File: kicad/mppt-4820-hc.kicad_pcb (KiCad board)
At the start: 4 copper layers, 100 x 100 mm, 141 parts, among them J1 MKDS 5/ 2-9,5, J2 MKDS 5/ 2-9,5, J4 8P8C, J5 8P8C, J7 UEXT, P1 CONN_01X02, Q1 IPA045N10N3G, Q2 IPA045N10N3G, Q3 IPA045N10N3G, T1 BC846B, T10 BC846B, T3 BC846B, T4 BC856B, U1 LM5107, U2 STM32G431CBTx, U3 MPQ8112, U4 LMR16006X, U6 W25Q80DVS, U7 TCAN334, Y1 8MHz

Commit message: pcb minor fixes, updated bom files, updated project name
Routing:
- net /CAN_GND: track 129.5 -> 127.1 mm
- net /CAN/CAN_PWR1: track 103.0 -> 100.8 mm
- net VBUS: vias 20 -> 24
- net /BAT+: vias 4 -> 8
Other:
- board text added: "MPPT 4820 HC"
- board text added: "v0.1.0"
- board text removed: "MPPT 2420 HC"
- board text removed: "v0.2.3"

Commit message: minor fixes & cleanup
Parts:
- moved J2 0.12 mm to (145.2, 132.0)
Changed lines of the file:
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@@
   )
   (footprint "LibreSolar:Phoenix_Contact_MKDS_5-2-9,5" (layer "F.Cu")
-    (at 145.139 132.05)
+    (at 145.25 132)
     (descr "Phoenix Contact MKDS 5/2-9,52")
     (property "Manufacturer" "Phoenix Contact")

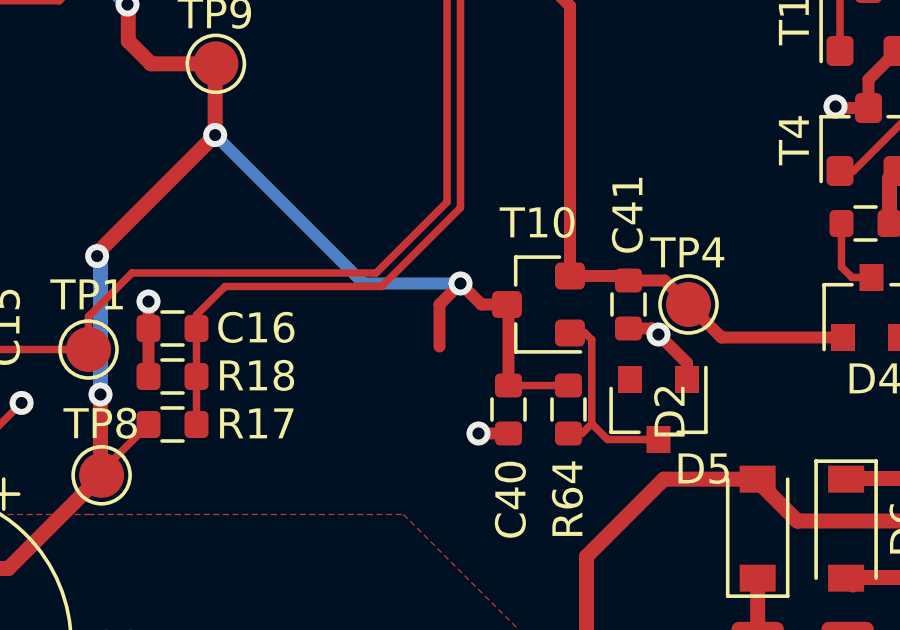
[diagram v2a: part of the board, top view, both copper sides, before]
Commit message: updated project to kicad 7
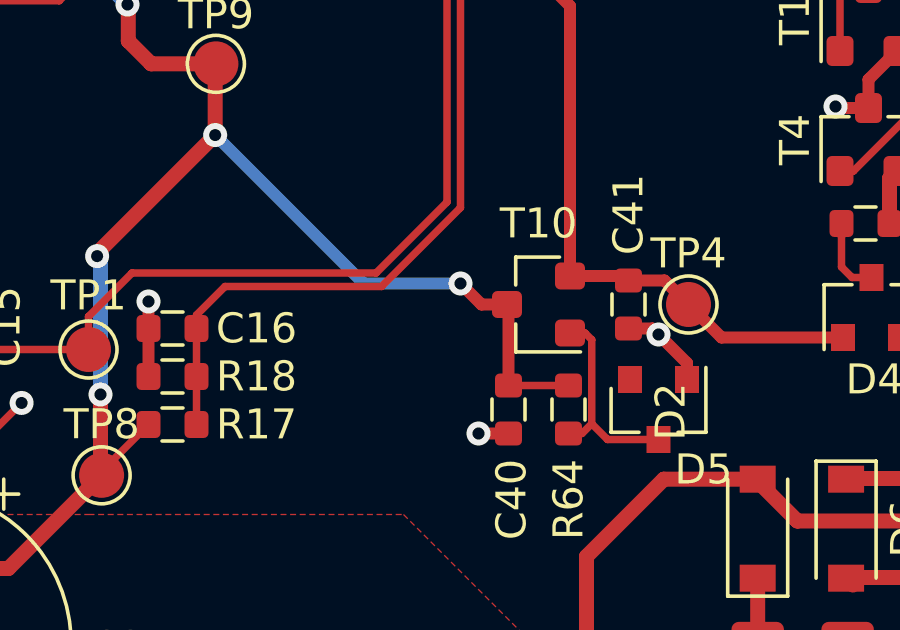
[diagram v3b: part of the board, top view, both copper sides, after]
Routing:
- net VBUS: track 124.3 -> 122.0 mm

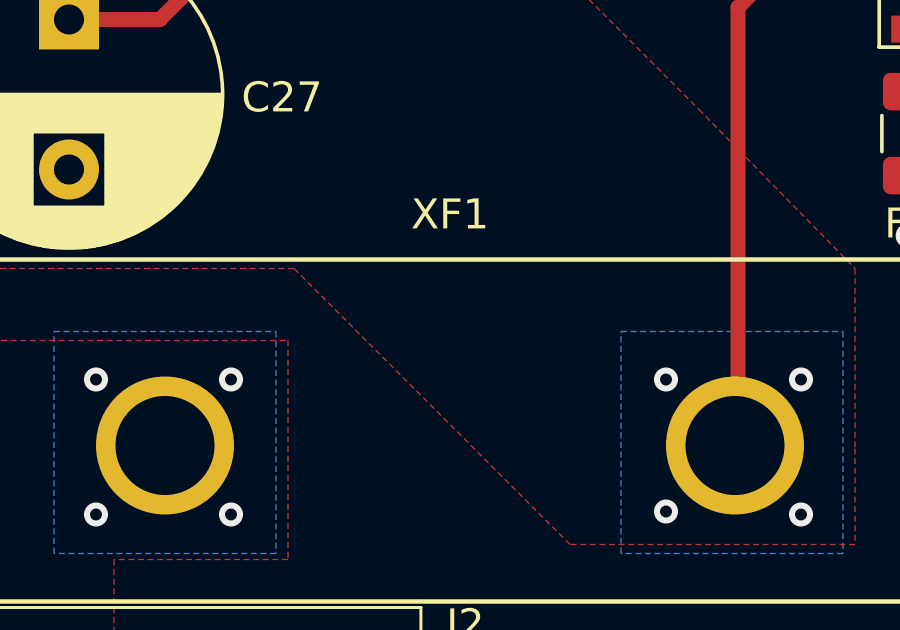
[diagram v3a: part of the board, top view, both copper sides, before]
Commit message: some DRC check errors fixes (prototype 1)
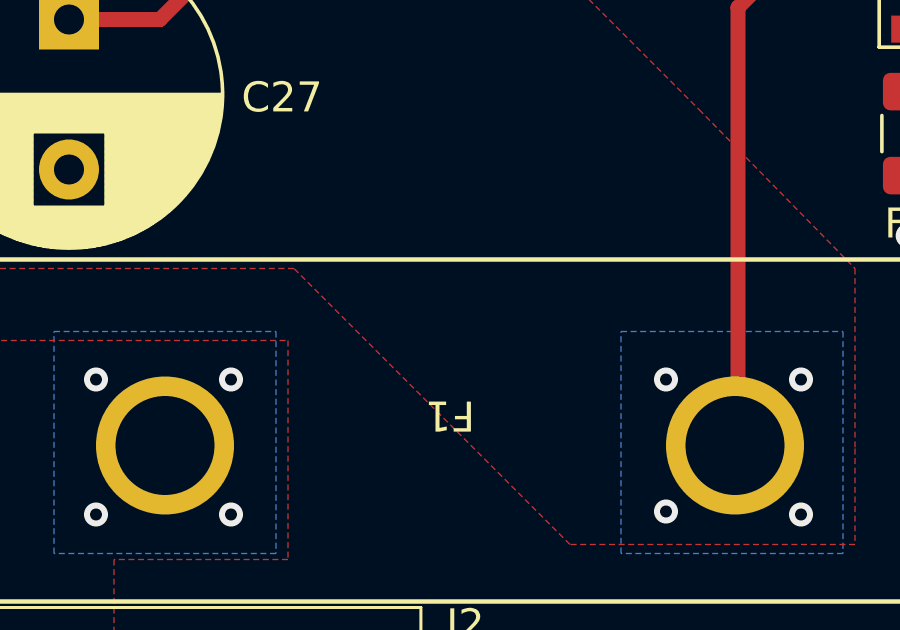
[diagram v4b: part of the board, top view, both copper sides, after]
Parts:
- removed XF1: Fuse_Holder, LibreSolar:Eaton_S-4000
- F1: footprint LibreSolar:NULL -> LibreSolar:Eaton_S-4000
- moved F1 13.6 mm to (160.5, 122.0)
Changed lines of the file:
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@@
     )
   )
-  (footprint "LibreSolar:NULL" (layer "F.Cu")
-    (at 147 123.5 180)
+  (footprint "LibreSolar:Eaton_S-4000" (layer "F.Cu")
+    (at 160.5 122 180)
     (property "Manufacturer" "Littelfuse")
     (property "PartNumber" "0287025.PXCN")
     (property "Sheetfile" "mppt-4820-hc.kicad_sch")
     (property "Sheetname" "")
-    (attr exclude_from_pos_files)
-    (fp_text reference "F1" (at 0 1) (layer "F.SilkS") hide
+    (attr through_hole)
+    (fp_text reference "F1" (at 0 1 180 unlocked) (layer "F.SilkS")
         (effects (font (size 1 1) (thickness 0.15)))
     )
-    (fp_text value "25A" (at 0 -1) (layer "F.Fab") hide
+    (fp_text value "25A" (at 0 -7 180 unlocked) (layer "F.Fab")
         (effects (font (size 1 1) (thickness 0.15)))
     )
+    (fp_rect (start -17.2 -5.2) (end 17.2 6.2)
+      (stroke (width 0.15) (type solid)) (fill none) (layer "F.SilkS"))
+    (fp_rect (start -17 -5) (end 17 6)
+      (stroke (width 0.12) (type solid)) (fill none) (layer "F.Fab"))
+    (pad "1" thru_hole circle (at -9.5 0 180) (size 4.6 4.6) (drill 3.3) (layers "*.Cu" "*.Mask")
+      (net 37 "VBUS"))
+    (pad "2" thru_hole circle (at 9.5 0 180) (size 4.6 4.6) (drill 3.3) (layers "*.Cu" "*.Mask")
+      (net 31 "/BAT+"))
   )
   (footprint "LibreSolar:R_0805_2012" (layer "F.Cu")
@@
     (property "ki_description" "Two pin crystal")
     (property "ki_keywords" "Quartz, Resonator, Ceramic, Filter")
-    (attr through_hole)
+    (attr smd)
     (fp_text reference "Y1" (at 3 0 90) (layer "F.SilkS")
         (effects (font (size 1 1) (thickness 0.15)))
@@
     )
   )
-  (footprint "LibreSolar:Eaton_S-4000" (layer "F.Cu")
-    (at 160.5 122 180)
-    (property "Manufacturer" "Eaton")
-    (property "PartNumber" "")
-    (property "Sheetfile" "mppt-4820-hc.kicad_sch")
-    (property "Sheetname" "")
-    (attr smd)
-    (fp_text reference "XF1" (at 0 7.7 unlocked) (layer "F.SilkS")
-        (effects (font (size 1 1) (thickness 0.15)))
-    )
-    (fp_text value "Fuse_Holder" (at 0 -6 180 unlocked) (layer "F.Fab")
-        (effects (font (size 1 1) (thickness 0.15)))
-    )
-    (fp_rect (start -17.2 -5.2) (end 17.2 6.2)
-      (stroke (width 0.15) (type solid)) (fill none) (layer "F.SilkS"))
-    (fp_rect (start -17.2 -5.2) (end 17.2 6.2)
-      (stroke (width 0.12) (type solid)) (fill none) (layer "F.Fab"))
-    (pad "1" thru_hole circle (at -9.5 0 180) (size 4.6 4.6) (drill 3.3) (layers "*.Cu" "*.Mask")
-      (net 37 "VBUS") (pintype "passive"))
-    (pad "2" thru_hole circle (at 9.5 0 180) (size 4.6 4.6) (drill 3.3) (layers "*.Cu" "*.Mask")
-      (net 31 "/BAT+") (pintype "passive"))
-  )
   (footprint "Connector_PinHeader_2.54mm:PinHeader_1x02_P2.54mm_Vertical" (layer "F.Cu")
     (at 196.99 67.61)
@@
   (via (at 137 133.5) (size 0.8) (drill 0.4) (layers "F.Cu" "B.Cu") (net 38))
   (via (at 127.25 119.75) (size 0.8) (drill 0.4) (layers "F.Cu" "B.Cu") (net 38))
-  (via (at 135 124) (size 0.8) (drill 0.4) (layers "F.Cu" "B.Cu") (net 38))
+  (via (at 135 124) (size 0.8) (drill 0.4) (layers "F.Cu" "B.Cu") (free) (net 38))
   (via (at 129.75 119.75) (size 0.8) (drill 0.4) (layers "F.Cu" "B.Cu") (net 38))
   (via (at 134.5 130.5) (size 0.8) (drill 0.4) (layers "F.Cu" "B.Cu") (net 38))
